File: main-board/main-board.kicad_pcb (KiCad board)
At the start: 2 copper layers, 117 x 83 mm, 72 parts, among them J1 NVIDIA_Jetson_NX_Dev_40pin_Co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, J10 FSESC_6.6_COMM_Minimal, J11 FSESC_6.6_COMM_Minimal, J12 FSESC_6.6_COMM_Minimal, J13 FSESC_6.6_COMM_Minimal, J14 ArducamPTZ, J15 Angle Sensor, J2 NVIDIA_Jetson_NX_Dev_Button_C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, J3 Conn_01x02, J4 Conn_01x02, J5 Conn_01x02, J6 FSESC_6.6_COMM_Minimal, J7 QWIIC_Generic_Conn, J8 Conn_01x03, J9 FSESC_6.6_COMM_Minimal, M1 Fan_3pin, M2 Fan_3pin, M3 Fan_3pin, Q1 Q_NMOS_GSD, Q2 Q_NMOS_GSD, Q4 Q_NMOS_GSD, Q5 Q_NMOS_GSD, Q6 Q_NMOS_GSD, Q7 Q_NMOS_GSD, Q8 Q_NMOS_GSD, U1 RFM95W_Adafruit_Breakout, U10 Analog Temp Sensor, U11 Adafruit_GPS_V3, U12 SN74AHCT125D, U2 TDK_I3A4W008A033V, U3 TDK_I3A4W008A033V, U5 Teensy_4.1, U6 Analog Temp Sensor, U7 Analog Temp Sensor, U8 Analog Temp Sensor, U9 Analog Temp Sensor

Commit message: XT60 Fix
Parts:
- BT1: value Battery -> XT60_Battery_Connector
- moved BT1 7.20 mm to (169.0, 65.8), turned to 270 degrees
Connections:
- BT1 pad 1: +BATT -> GND
- BT1 pad 2: GND -> +BATT
- J1 pad 1: (no net) -> Net-(J1-Pad1)
- J1 pad 10: (no net) -> Net-(J1-Pad10)
- J1 pad 11: (no net) -> Net-(J1-Pad11)
- J1 pad 12: (no net) -> Net-(J1-Pad12)
- J1 pad 13: (no net) -> Net-(J1-Pad13)
- J1 pad 15: (no net) -> Net-(J1-Pad15)
- J1 pad 16: (no net) -> Net-(J1-Pad16)
- J1 pad 17: (no net) -> Net-(J1-Pad17)
- J1 pad 18: (no net) -> Net-(J1-Pad18)
- J1 pad 19: (no net) -> Net-(J1-Pad19)
- J1 pad 2: (no net) -> Net-(J1-Pad2)
- J1 pad 21: (no net) -> Net-(J1-Pad21)
- J1 pad 22: (no net) -> Net-(J1-Pad22)
- J1 pad 23: (no net) -> Net-(J1-Pad23)
- J1 pad 24: (no net) -> Net-(J1-Pad24)
- J1 pad 26: (no net) -> Net-(J1-Pad26)
- J1 pad 27: (no net) -> Net-(J1-Pad27)
- J1 pad 28: (no net) -> Net-(J1-Pad28)
- J1 pad 29: (no net) -> Net-(J1-Pad29)
- J1 pad 31: (no net) -> Net-(J1-Pad31)
- J1 pad 32: (no net) -> Net-(J1-Pad32)
- J1 pad 33: (no net) -> Net-(J1-Pad33)
- J1 pad 35: (no net) -> Net-(J1-Pad35)
- J1 pad 36: (no net) -> Net-(J1-Pad36)
- J1 pad 37: (no net) -> Net-(J1-Pad37)
- J1 pad 38: (no net) -> Net-(J1-Pad38)
- J1 pad 4: (no net) -> Net-(J1-Pad4)
- J1 pad 40: (no net) -> Net-(J1-Pad40)
- J1 pad 7: (no net) -> Net-(J1-Pad7)
- J1 pad 8: (no net) -> Net-(J1-Pad8)
- J2 pad 10: (no net) -> Net-(J2-Pad10)
- J2 pad 3: (no net) -> Net-(J2-Pad3)
- J2 pad 4: (no net) -> Net-(J2-Pad4)
- J2 pad 5: (no net) -> Net-(J2-Pad5)
- J2 pad 6: (no net) -> Net-(J2-Pad6)
- M1 pad 3: (no net) -> Net-(M1-Pad3)
- M2 pad 3: (no net) -> Net-(M2-Pad3)
- M3 pad 3: (no net) -> Net-(M3-Pad3)
- U1 pad 11: (no net) -> Net-(U1-Pad11)
- U1 pad 12: (no net) -> Net-(U1-Pad12)
- U1 pad 13: (no net) -> Net-(U1-Pad13)
- U1 pad 14: (no net) -> Net-(U1-Pad14)
- U1 pad 15: (no net) -> Net-(U1-Pad15)
- U1 pad 3: (no net) -> Net-(U1-Pad3)
- U11 pad 1: (no net) -> Net-(U11-Pad1)
- U11 pad 2: (no net) -> Net-(U11-Pad2)
- U11 pad 3: (no net) -> Net-(U11-Pad3)
- U11 pad 4: (no net) -> Net-(U11-Pad4)
- U11 pad 9: (no net) -> Net-(U11-Pad9)
- U2 pad 5: (no net) -> Net-(U2-Pad5)
- U3 pad 5: (no net) -> Net-(U3-Pad5)
- U5 pad 15: (no net) -> Net-(U5-Pad15)
- U5 pad 20: (no net) -> Net-(U5-Pad20)
- U5 pad 21: (no net) -> Net-(U5-Pad21)
- U5 pad 26: (no net) -> Net-(U5-Pad26)
- U5 pad 27: (no net) -> Net-(U5-Pad27)
- U5 pad 39: (no net) -> Net-(U5-Pad39)

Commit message: Probably should do a rev increase
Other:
- board text added: "UAH SHC ASTRA Rover PCB V1.1 Sep 2021"
- board text removed: "UAH SHC ASTRA Rover PCB V1 Sep 2021"

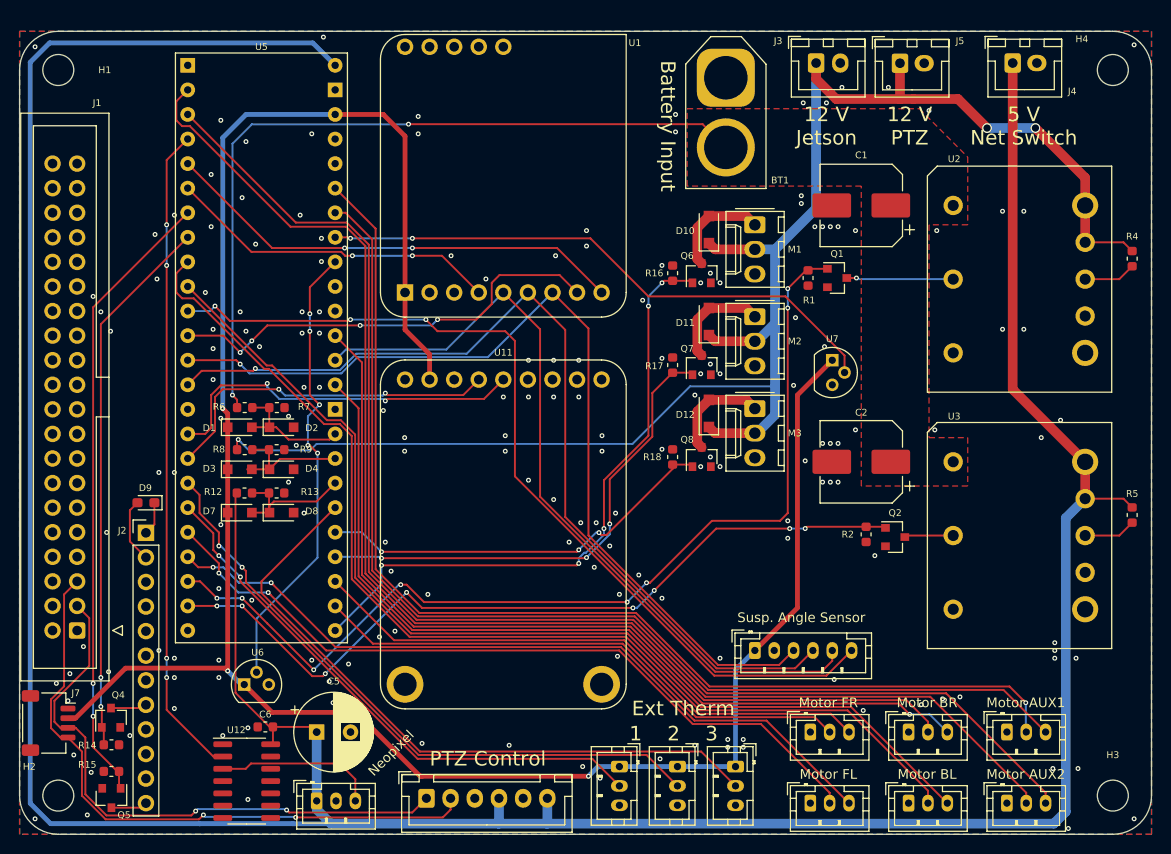
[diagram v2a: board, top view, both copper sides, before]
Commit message: Implemented post SAR fixes
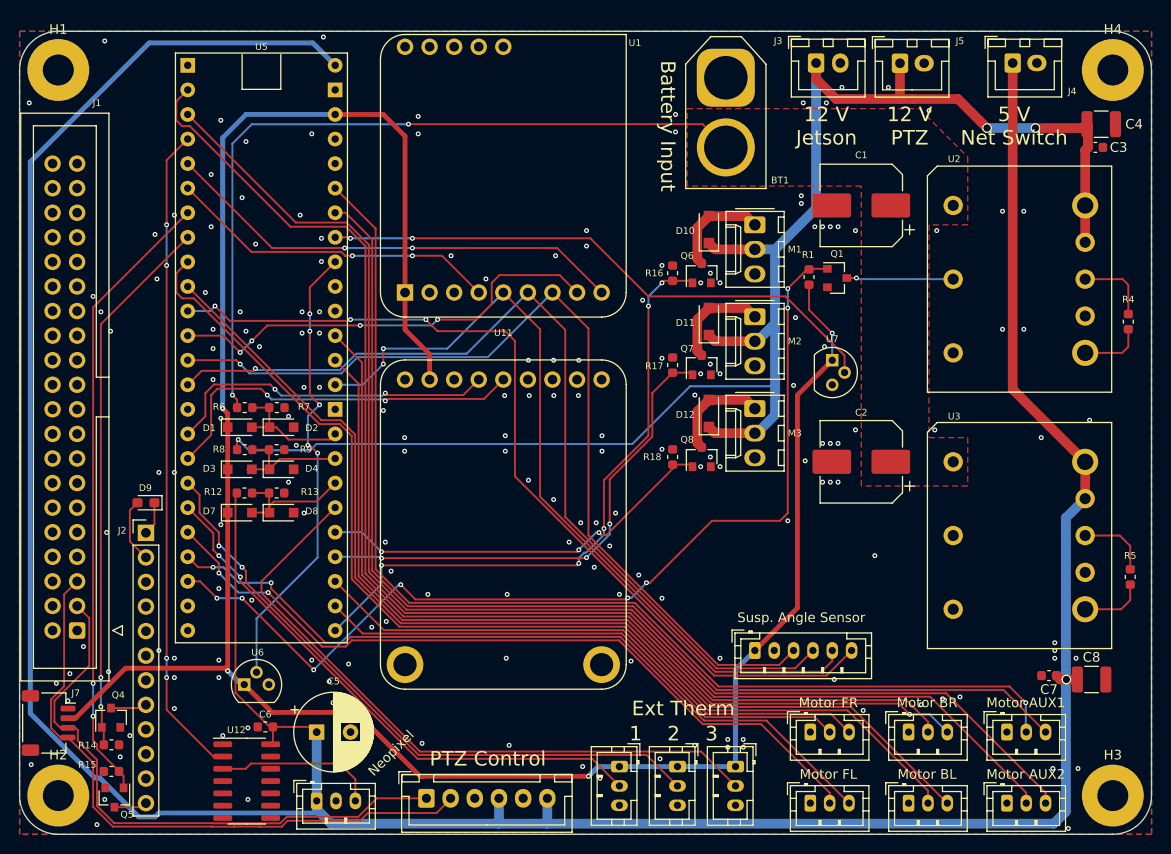
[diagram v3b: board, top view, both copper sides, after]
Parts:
- removed Q2: Q_NMOS_GSD, Package_TO_SOT_SMD:SOT-23
- removed R2: 100k, Resistor_SMD:R_0603_1608Metric
- added C3: 0.1u, Capacitor_SMD:C_0603_1608Metric, F.Cu at (207.2, 73.0)
- added C4: 22u, Capacitor_SMD:C_1210_3225Metric, F.Cu at (207.8, 70.6)
- added C7: 0.1u, Capacitor_SMD:C_0603_1608Metric, F.Cu at (202.4, 127.6)
- added C8: 22u, Capacitor_SMD:C_1210_3225Metric, F.Cu at (206.8, 128.0)
- H1, H2, H3, H4: footprint MountingHole:MountingHole_3.2mm_M3 -> MountingHole:MountingHole_3.2mm_M3_Pad
- moved R4 6.52 mm to (210.6, 91.0)
- moved R5 6.40 mm to (210.8, 117.4)
- moved Q5 0.31 mm to (105.8, 140.2)
- moved R1 0.14 mm to (177.6, 86.4), turned to 90 degrees
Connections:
- R1 pad 1: /12V_Disable -> +3V3
- R1 pad 2: GND -> /12V_Disable
- R4 pad 1: +12V -> Net-(R4-Pad1)
- R4 pad 2: Net-(R4-Pad2) -> GND
- R5 pad 1: +5V -> Net-(R5-Pad1)
- R5 pad 2: Net-(R5-Pad2) -> GND
- U2 pad 6: Net-(R4-Pad2) -> Net-(R4-Pad1)
- U3 pad 2: Net-(Q2-Pad3) -> GND
- U3 pad 6: Net-(R5-Pad2) -> Net-(R5-Pad1)
- U5 pad 17: /M3_TX -> /SCK
- U5 pad 18: /SCK -> /M3_TX
- U5 pad 31: /GPS_TX -> /GPS_RX
- U5 pad 32: /GPS_RX -> /GPS_TX
- U5 pad 38: /5V_Disable -> Net-(U5-Pad38)
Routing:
- net /5V_Disable: track 82.9 -> 0.00 mm, vias 8 -> 0
- net +5V: track 352.9 -> 338.8 mm, vias 0 -> 1
- net GND: track 0.00 -> 13.2 mm
- net +3V3: track 224.6 -> 233.4 mm, vias 3 -> 4
- net Net-(R4-Pad1): track 0.00 -> 7.73 mm
- net Net-(R5-Pad1): track 0.00 -> 7.52 mm
- net Net-(R5-Pad2): track 5.41 -> 0.00 mm
- net Net-(R4-Pad2): track 5.41 -> 0.00 mm
- net Net-(Q2-Pad3): track 5.07 -> 0.00 mm
- net /M3_TX: track 88.3 -> 90.9 mm
- net /SCK: track 82.2 -> 84.2 mm, vias 0 -> 2
- net +12V: track 170.1 -> 168.8 mm
- net /GPS_RX: track 36.2 -> 34.9 mm
- net /M2_TX: track 78.9 -> 79.7 mm
- net /GPS_TX: track 38.6 -> 39.5 mm
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
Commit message: I changed something?
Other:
- board text added: "UAH SHC ASTRA Rover PCB V1.2 Mar 2022"
- board text removed: "UAH SHC ASTRA Rover PCB V1.1 Sep 2021"

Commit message: something?
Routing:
- net GND: vias 178 -> 206

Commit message: Indicator LEDs
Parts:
- added D13: G, LED_SMD:LED_0603_1608Metric_Pad1.05x0.95mm_HandSolder, F.Cu at (193.5, 66.6)
- added D14: G, LED_SMD:LED_0603_1608Metric_Pad1.05x0.95mm_HandSolder, F.Cu at (160.2, 68.4)
- added D5: G, LED_SMD:LED_0603_1608Metric_Pad1.05x0.95mm_HandSolder, F.Cu at (110.2, 67.0)
- added D6: G, LED_SMD:LED_0603_1608Metric_Pad1.05x0.95mm_HandSolder, F.Cu at (107.6, 67.0)
- added R10: 1k, Resistor_SMD:R_0603_1608Metric, F.Cu at (193.5, 63.4)
- added R11: 3.3k, Resistor_SMD:R_0603_1608Metric, F.Cu at (160.2, 65.2)
- added R2: 10, Resistor_SMD:R_0603_1608Metric, F.Cu at (110.2, 70.2)
- added R3: 180, Resistor_SMD:R_0603_1608Metric, F.Cu at (107.6, 70.2)
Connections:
- J1 pad 1: Net-(J1-Pad1) -> (no net)
- J1 pad 10: Net-(J1-Pad10) -> (no net)
- J1 pad 11: Net-(J1-Pad11) -> (no net)
- J1 pad 12: Net-(J1-Pad12) -> (no net)
- J1 pad 13: Net-(J1-Pad13) -> (no net)
- J1 pad 15: Net-(J1-Pad15) -> (no net)
- J1 pad 16: Net-(J1-Pad16) -> (no net)
- J1 pad 17: Net-(J1-Pad17) -> (no net)
- J1 pad 18: Net-(J1-Pad18) -> (no net)
- J1 pad 19: Net-(J1-Pad19) -> (no net)
- J1 pad 2: Net-(J1-Pad2) -> (no net)
- J1 pad 21: Net-(J1-Pad21) -> (no net)
- J1 pad 22: Net-(J1-Pad22) -> (no net)
- J1 pad 23: Net-(J1-Pad23) -> (no net)
- J1 pad 24: Net-(J1-Pad24) -> (no net)
- J1 pad 26: Net-(J1-Pad26) -> (no net)
- J1 pad 27: Net-(J1-Pad27) -> (no net)
- J1 pad 28: Net-(J1-Pad28) -> (no net)
- J1 pad 29: Net-(J1-Pad29) -> (no net)
- J1 pad 31: Net-(J1-Pad31) -> (no net)
- J1 pad 32: Net-(J1-Pad32) -> (no net)
- J1 pad 33: Net-(J1-Pad33) -> (no net)
- J1 pad 35: Net-(J1-Pad35) -> (no net)
- J1 pad 36: Net-(J1-Pad36) -> (no net)
- J1 pad 37: Net-(J1-Pad37) -> (no net)
- J1 pad 38: Net-(J1-Pad38) -> (no net)
- J1 pad 4: Net-(J1-Pad4) -> (no net)
- J1 pad 40: Net-(J1-Pad40) -> (no net)
- J1 pad 7: Net-(J1-Pad7) -> (no net)
- J1 pad 8: Net-(J1-Pad8) -> (no net)
- J2 pad 10: Net-(J2-Pad10) -> (no net)
- J2 pad 3: Net-(J2-Pad3) -> (no net)
- J2 pad 4: Net-(J2-Pad4) -> (no net)
- J2 pad 5: Net-(J2-Pad5) -> (no net)
- J2 pad 6: Net-(J2-Pad6) -> (no net)
- M1 pad 3: Net-(M1-Pad3) -> (no net)
- M2 pad 3: Net-(M2-Pad3) -> (no net)
- M3 pad 3: Net-(M3-Pad3) -> (no net)
- U1 pad 11: Net-(U1-Pad11) -> (no net)
- U1 pad 12: Net-(U1-Pad12) -> (no net)
- U1 pad 13: Net-(U1-Pad13) -> (no net)
- U1 pad 14: Net-(U1-Pad14) -> (no net)
- U1 pad 15: Net-(U1-Pad15) -> (no net)
- U1 pad 3: Net-(U1-Pad3) -> (no net)
- U11 pad 1: Net-(U11-Pad1) -> (no net)
- U11 pad 2: Net-(U11-Pad2) -> (no net)
- U11 pad 3: Net-(U11-Pad3) -> (no net)
- U11 pad 4: Net-(U11-Pad4) -> (no net)
- U11 pad 9: Net-(U11-Pad9) -> (no net)
- U2 pad 5: Net-(U2-Pad5) -> (no net)
- U3 pad 5: Net-(U3-Pad5) -> (no net)
- U5 pad 15: Net-(U5-Pad15) -> (no net)
- U5 pad 20: Net-(U5-Pad20) -> (no net)
- U5 pad 21: Net-(U5-Pad21) -> (no net)
- U5 pad 26: Net-(U5-Pad26) -> (no net)
- U5 pad 27: Net-(U5-Pad27) -> (no net)
- U5 pad 38: Net-(U5-Pad38) -> (no net)
- U5 pad 39: Net-(U5-Pad39) -> (no net)
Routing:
- net +3V3: track 233.4 -> 250.8 mm, vias 4 -> 5
- net +5V: track 338.8 -> 340.7 mm, vias 1 -> 2
- net Net-(D6-Pad1): track 0.00 -> 1.50 mm
- net Net-(D5-Pad1): track 0.00 -> 1.50 mm
- net Net-(D14-Pad1): track 0.00 -> 1.50 mm
- net Net-(D13-Pad1): track 0.00 -> 1.50 mm
- net +BATT: track 80.3 -> 81.6 mm
- net +12V: track 168.8 -> 169.5 mm
- net GND: vias 206 -> 212
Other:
- board text added: "3v3"
- board text added: "5V"
